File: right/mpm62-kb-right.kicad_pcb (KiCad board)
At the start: 2 copper layers, 161.9 x 95.2 mm, 72 parts, among them J1 Conn_01x04_Male, SW1 SW_Push, U1 MCP23018-E_SP

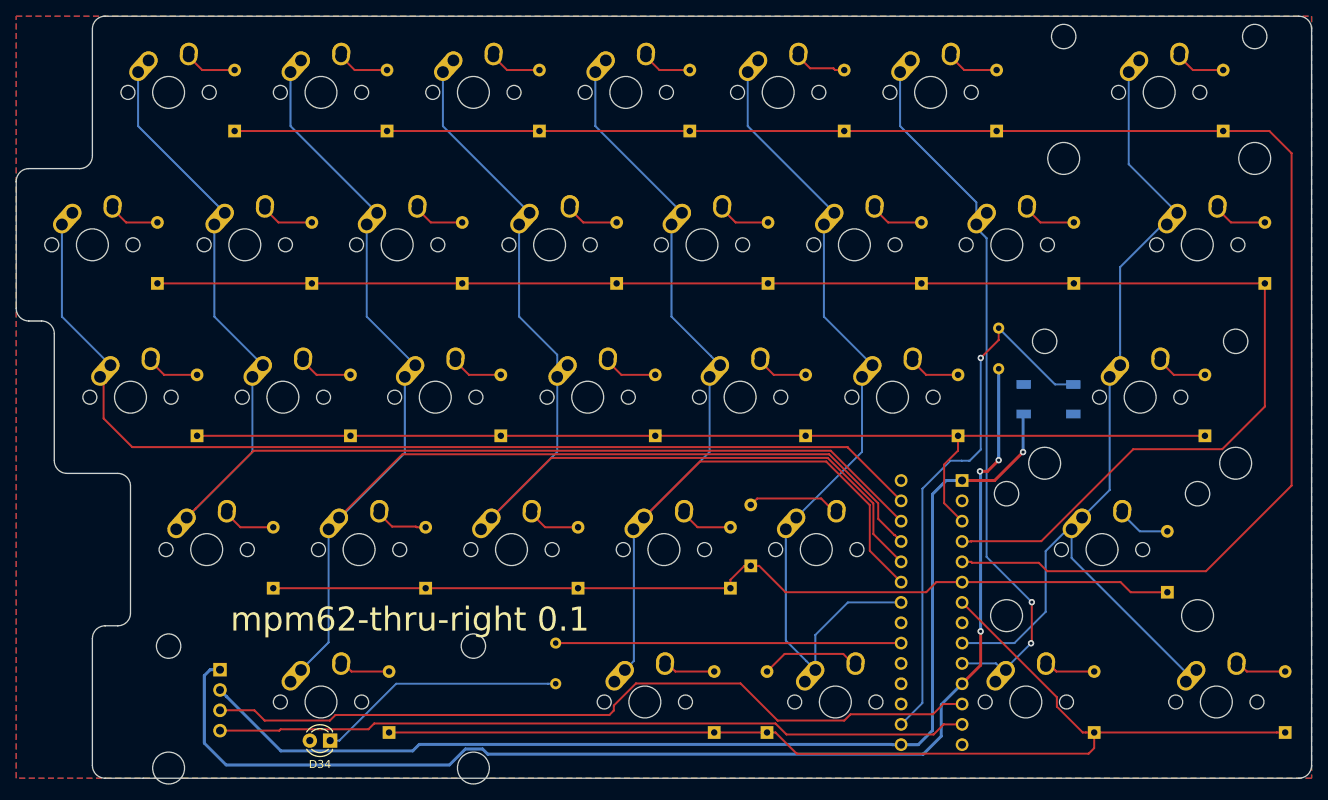
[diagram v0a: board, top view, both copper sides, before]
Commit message: Fix issues on right side: 1. Remove reset switch and connect reset directly to vcc - switch was not useful and added complexity. 2. Inverted spacebar stabilizer holes (previous commit did not mention that this was done also on the left side). 3. LED was connected to wrong power bus. 4. Resistor size was smaller than typical TH resistors. 5. Add header pins for ground and vcc for debugging. 6. Some minor routing cleanups.
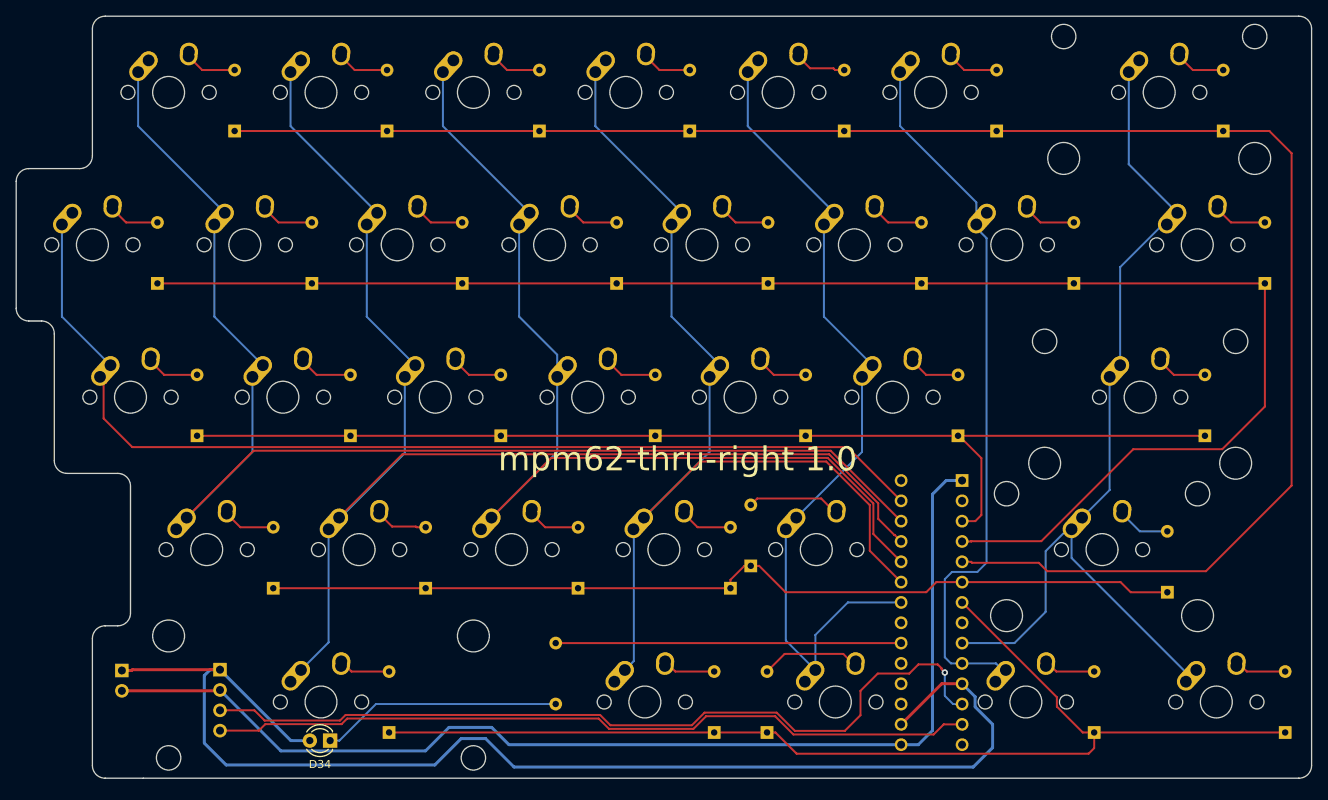
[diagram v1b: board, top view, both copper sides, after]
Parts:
- removed R2: R_Small, Resistor_THT:R_Axial_DIN0204_L3.6mm_D1.6mm_P5.08mm_Horizontal
- removed SW1: SW_Push, random-keyboard-parts:SKQG-1155865
- added J2: Conn_01x02_Male, Connector_PinHeader_2.54mm:PinHeader_1x02_P2.54mm_Vertical, B.Cu at (60.8, 129.4)
- MX1: value MX-NoLED -> Y
- MX10: value MX-NoLED -> M
- MX11: value MX-NoLED -> spc; footprint MX_Alps_Hybrid:MX-3U-NoLED -> MX_Alps_Hybrid:MX-3U-ReversedStabilizers-NoLED
- MX12: value MX-NoLED -> 9
- MX13: value MX-NoLED -> O
- MX14: value MX-NoLED -> L
- MX15: value MX-NoLED -> comma
- MX16: value MX-NoLED -> 0
- MX17: value MX-NoLED -> P
- MX18: value MX-NoLED -> semicolon
- MX19: value MX-NoLED -> period
- MX2: value MX-NoLED -> H
- MX20: value MX-NoLED -> ctrl
- MX21: value MX-NoLED -> hyphen
- MX22: value MX-NoLED -> lbracket
- MX23: value MX-NoLED -> quote
- MX24: value MX-NoLED -> slash
- MX25: value MX-NoLED -> fn
- MX26: value MX-NoLED -> equals
- MX27: value MX-NoLED -> rbracket
- MX28: value MX-NoLED -> menu
- MX29: value MX-NoLED -> backspc
- MX3: value MX-NoLED -> 7
- MX30: value MX-NoLED -> backslash
- MX31: value MX-NoLED -> enter
- MX32: value MX-NoLED -> shift
- MX33: value MX-NoLED -> alt
- MX4: value MX-NoLED -> U
- MX5: value MX-NoLED -> J
- MX6: value MX-NoLED -> N
- MX7: value MX-NoLED -> 8
- MX8: value MX-NoLED -> I
- MX9: value MX-NoLED -> K
- R1: value R_Small -> 100; footprint Resistor_THT:R_Axial_DIN0204_L3.6mm_D1.6mm_P5.08mm_Horizontal -> Resistor_THT:R_Axial_DIN0207_L6.3mm_D2.5mm_P7.62mm_Horizontal
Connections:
- D34 pad 2: (no net) -> VCC
- MX1 pad 1: COL6 -> COL7
- MX10 pad 1: COL8 -> COL9
- MX11 pad 1: COL8 -> COL9
- MX12 pad 1: COL9 -> COL10
- MX13 pad 1: COL9 -> COL10
- MX14 pad 1: COL9 -> COL10
- MX15 pad 1: COL9 -> COL10
- MX16 pad 1: COL10 -> COL11
- MX17 pad 1: COL10 -> COL11
- MX18 pad 1: COL10 -> COL11
- MX19 pad 1: COL10 -> COL11
- MX2 pad 1: COL6 -> COL7
- MX20 pad 1: COL10 -> COL11
- MX21 pad 1: COL11 -> COL12
- MX22 pad 1: COL11 -> COL12
- MX23 pad 1: COL11 -> COL12
- MX24 pad 1: COL11 -> COL12
- MX25 pad 1: COL11 -> COL12
- MX26 pad 1: COL12 -> COL13
- MX27 pad 1: COL12 -> COL13
- MX28 pad 1: COL12 -> COL13
- MX29 pad 1: COL13 -> COL14
- MX3 pad 1: COL7 -> COL8
- MX30 pad 1: COL13 -> COL14
- MX31 pad 1: COL13 -> COL14
- MX32 pad 1: COL13 -> COL14
- MX33 pad 1: COL13 -> COL14
- MX4 pad 1: COL7 -> COL8
- MX5 pad 1: COL7 -> COL8
- MX6 pad 1: COL7 -> COL8
- MX7 pad 1: COL8 -> COL9
- MX8 pad 1: COL8 -> COL9
- MX9 pad 1: COL8 -> COL9
- U1 pad 10: COL12 -> COL13
- U1 pad 16: Net-(R2-Pad2) -> VCC
- U1 pad 22: COL11 -> COL12
- U1 pad 23: COL10 -> COL11
- U1 pad 24: COL9 -> COL10
- U1 pad 25: COL8 -> COL9
- U1 pad 26: COL7 -> COL8
- U1 pad 27: COL6 -> COL7
- U1 pad 9: COL13 -> COL14
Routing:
- net COL6: track 130.5 -> 0.00 mm
- net COL14: track 0.00 -> 108.4 mm
- net Net-(R2-Pad2): track 68.2 -> 0.00 mm, vias 1 -> 0
- net COL9: track 130.0 -> 163.4 mm
- net COL7: track 161.6 -> 130.5 mm
- net COL11: track 99.1 -> 125.9 mm
- net COL13: track 108.4 -> 90.3 mm
- net COL12: track 90.7 -> 99.1 mm, vias 2 -> 0
- net Net-(J1-Pad3): track 98.4 -> 104.8 mm, vias 0 -> 1
- net VCC: track 155.5 -> 160.9 mm, vias 3 -> 0
- net COL10: track 125.9 -> 130.0 mm
- net Net-(J1-Pad4): track 94.2 -> 96.0 mm
- net COL8: track 163.4 -> 161.6 mm
- net ROW2: track 138.9 -> 140.5 mm
- net Net-(D34-Pad1): track 31.1 -> 30.1 mm
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- removed copper zone on B.Cu, net GND
- removed copper zone on F.Cu, net GND
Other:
- board text added: "mpm62-thru-right 1.0"
- board text removed: "mpm62-thru-right 0.1"

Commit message: Final for b1t (board 1 thruhole) board
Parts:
- added G***: LOGO, MpmMisc:small_logo, B.Cu at (98.4, 124.6)
- added G***: LOGO, MpmMisc:biglogo3, F.Cu at (136.5, 92.6)
- added H1: MountingHole, MountingHole:MountingHole_2.2mm_M2_Pad, B.Cu at (66.7, 66.7)
- added H2: MountingHole, MountingHole:MountingHole_2.2mm_M2_Pad, B.Cu at (71.4, 126.2)
- added H3: MountingHole, MountingHole:MountingHole_2.2mm_M2_Pad, B.Cu at (184.2, 76.2)
- added H4: MountingHole, MountingHole:MountingHole_2.2mm_M2_Pad, B.Cu at (185.7, 133.3)
- added U2: TRRS, Keebio-Parts:TRRS-PJ-320A, B.Cu at (61.2, 126.0)
- J1: value Conn_01x04_Male -> Raw Header
- J2: value Conn_01x02_Male -> JST ZH Header; footprint Connector_PinHeader_2.54mm:PinHeader_1x02_P2.54mm_Vertical -> MpmMisc:JST_ZH_B4B-ZR_1x04_P1.50mm_Vertical
- MX1, MX10, MX12, MX13, MX14, MX15, MX16, MX17, MX18, MX19, MX2, MX21, MX22, MX23, MX24, MX26, MX27, MX3, MX4, MX5, MX6, MX7, MX8, MX9: footprint MX_Alps_Hybrid:MX-1U-NoLED -> MX_Only:MXOnly-1U-NoLED
- MX11: footprint MX_Alps_Hybrid:MX-3U-ReversedStabilizers-NoLED -> MX_Only:MXOnly-3U-ReversedStabilizers-NoLED
- MX20, MX25, MX28, MX33: footprint MX_Alps_Hybrid:MX-1.25U-NoLED -> MX_Only:MXOnly-1.25U-NoLED
- MX29: footprint MX_Alps_Hybrid:MX-2U-NoLED -> MX_Only:MXOnly-2U-NoLED
- MX30: footprint MX_Alps_Hybrid:MX-1.5U-NoLED -> MX_Only:MXOnly-1.5U-NoLED
- MX31: footprint MX_Alps_Hybrid:MX-2.25U-NoLED -> MX_Only:MXOnly-2.25U-NoLED
- MX32: footprint MX_Alps_Hybrid:MX-2.75U-NoLED -> MX_Only:MXOnly-2.75U-NoLED
- moved J2 10.9 mm to (71.6, 130.9), turned to 270 degrees
- moved D28 6.98 mm to (182.4, 130.2)
- moved J1 3.10 mm to (76.2, 129.4)
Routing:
- net Net-(J1-Pad4): track 96.0 -> 115.0 mm
- net Net-(J1-Pad3): track 104.8 -> 116.2 mm, vias 1 -> 0
- net GND: track 141.3 -> 152.7 mm
- net ROW4: track 139.3 -> 150.3 mm
- net COL11: track 125.9 -> 133.6 mm
- net COL8: track 161.6 -> 167.9 mm
- net COL9: track 163.4 -> 169.1 mm
- net COL14: track 108.4 -> 113.0 mm
- net COL12: track 99.1 -> 103.2 mm
- net Net-(D28-Pad2): track 6.53 -> 8.37 mm
- net COL10: track 130.0 -> 130.9 mm
- net COL7: track 130.5 -> 131.4 mm
- net COL13: track 90.3 -> 89.6 mm
- added copper zone on B.Cu, net GND
- added copper zone on F.Cu, net GND
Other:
- board text added: "minke·io b1t-right 1.0"
- board text removed: "mpm62-thru-right 1.0"
